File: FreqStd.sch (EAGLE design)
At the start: 33 parts, among them J1 ISP Connector, J2 BNC_RIGHT-ANGLE, SW1 PWR, U1 ATMEGA328, U2 MIC5205, U3 SN74LV164APW

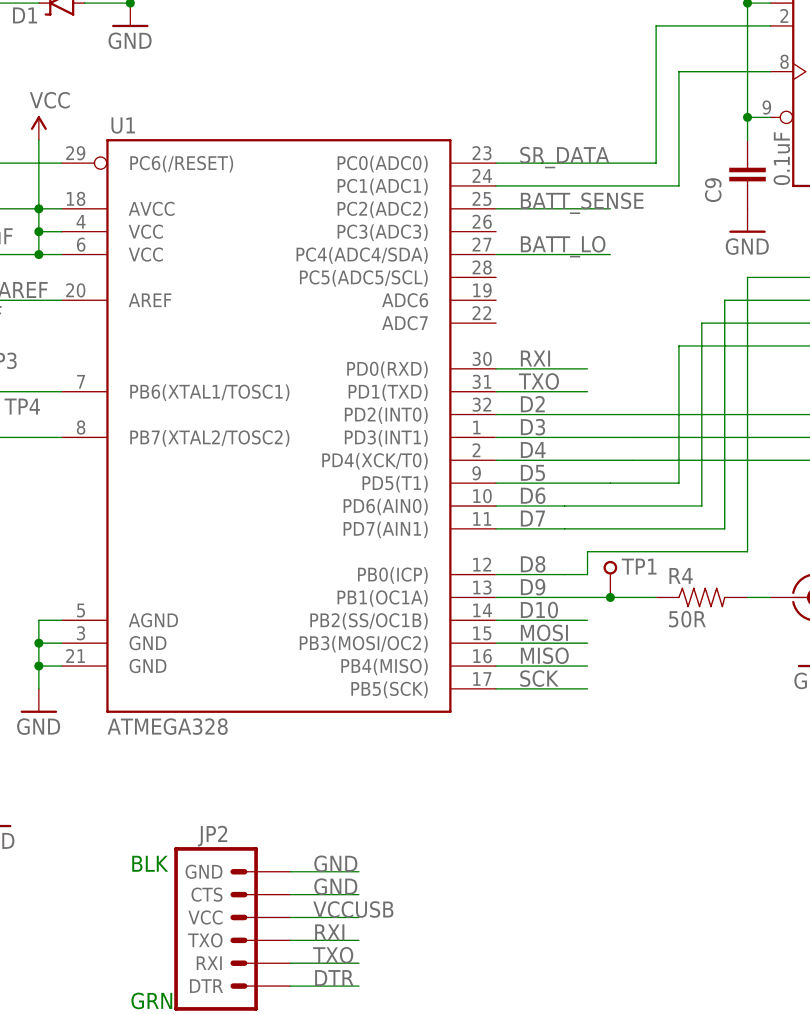
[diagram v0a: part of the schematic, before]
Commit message: Rev A board as ordered
Minor changes for ordering.  Added OSHPark renderings.  Started writing
firmware and GitHub cover.
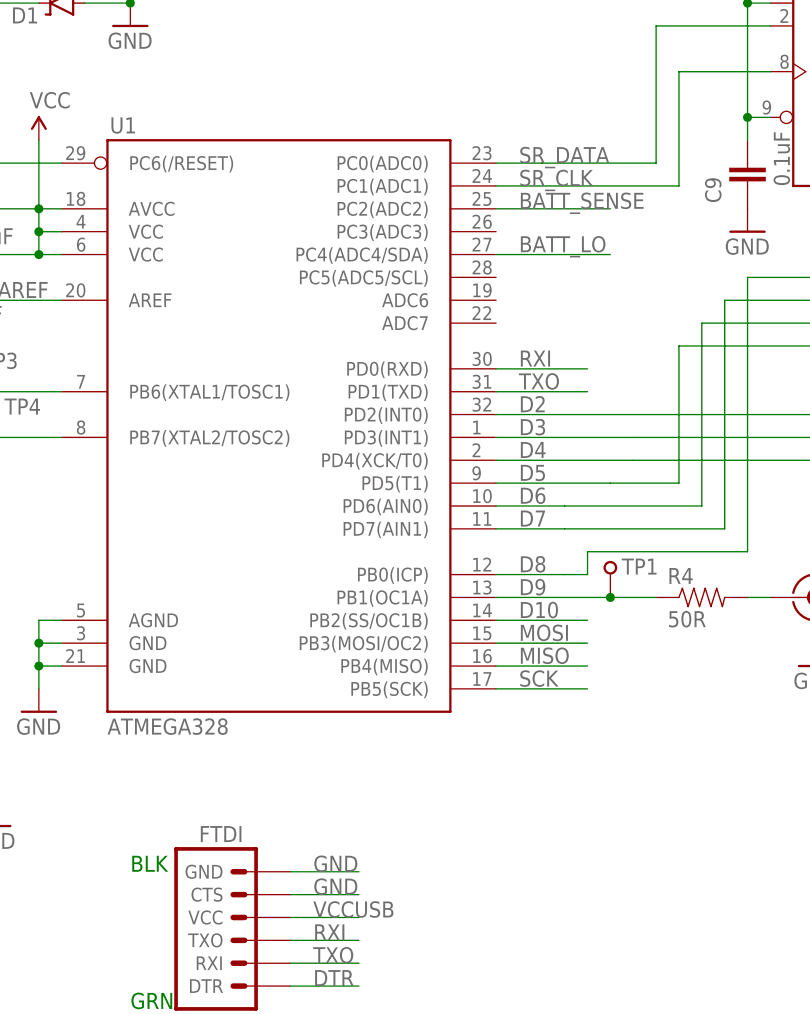
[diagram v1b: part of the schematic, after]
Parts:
- FRAME1: DATECODE 27AUG2015 -> 02SEP2015
- renumbered JP2 to FTDI
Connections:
- net N$7 renamed SR_CLK
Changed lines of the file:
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@@
 <?xml version="1.0" encoding="utf-8"?>
 <!DOCTYPE eagle SYSTEM "eagle.dtd">
-<eagle version="7.3.0">
+<eagle version="7.4.0">
 <drawing>
 <settings>
@@
 <part name="SUPPLY4" library="SparkFun-Aesthetics" deviceset="VCC" device="" value="VCC"/>
 <part name="GND4" library="SparkFun" deviceset="GND" device=""/>
-<part name="JP2" library="SparkFun" deviceset="ARDUINO_SERIAL_PROGRAM" device="PTH" value="FTDI Basic"/>
+<part name="FTDI" library="SparkFun" deviceset="ARDUINO_SERIAL_PROGRAM" device="PTH" value="FTDI Basic"/>
 <part name="J1" library="SparkFun-Connectors" deviceset="AVR_SPI_PRG_6" device="PTH" value="ISP Connector"/>
 <part name="SUPPLY3" library="SparkFun-Aesthetics" deviceset="VCC" device="" value="VCC"/>
@@
 <attribute name="CNAME" value="Frequency Standard"/>
 <attribute name="CREVISION" value="Rev A"/>
-<attribute name="DATECODE" value="27AUG2015"/>
+<attribute name="DATECODE" value="02SEP2015"/>
 <attribute name="DESIGNER" value="C.Schnarel"/>
 </part>
@@
 <instance part="SUPPLY4" gate="G$1" x="63.5" y="116.84"/>
 <instance part="GND4" gate="1" x="63.5" y="53.34"/>
-<instance part="JP2" gate="G$1" x="86.36" y="27.94"/>
+<instance part="FTDI" gate="G$1" x="86.36" y="27.94"/>
 <instance part="J1" gate="G$1" x="40.64" y="50.8"/>
 <instance part="SUPPLY3" gate="G$1" x="53.34" y="55.88"/>
@@
 <wire x1="91.44" y1="33.02" x2="99.06" y2="33.02" width="0.1524" layer="91"/>
 <label x="93.98" y="33.02" size="1.778" layer="95"/>
-<pinref part="JP2" gate="G$1" pin="CTS"/>
+<pinref part="FTDI" gate="G$1" pin="CTS"/>
 </segment>
 <segment>
 <wire x1="91.44" y1="35.56" x2="99.06" y2="35.56" width="0.1524" layer="91"/>
 <label x="93.98" y="35.56" size="1.778" layer="95"/>
-<pinref part="JP2" gate="G$1" pin="GND"/>
+<pinref part="FTDI" gate="G$1" pin="GND"/>
 </segment>
 <segment>
@@
 <wire x1="91.44" y1="25.4" x2="99.06" y2="25.4" width="0.1524" layer="91"/>
 <label x="93.98" y="25.4" size="1.778" layer="95"/>
-<pinref part="JP2" gate="G$1" pin="RXI"/>
+<pinref part="FTDI" gate="G$1" pin="RXI"/>
 </segment>
 </net>
@@
 <wire x1="91.44" y1="22.86" x2="99.06" y2="22.86" width="0.1524" layer="91"/>
 <label x="93.98" y="22.86" size="1.778" layer="95"/>
-<pinref part="JP2" gate="G$1" pin="DTR"/>
+<pinref part="FTDI" gate="G$1" pin="DTR"/>
 </segment>
 <segment>
@@
 <wire x1="91.44" y1="27.94" x2="99.06" y2="27.94" width="0.1524" layer="91"/>
 <label x="93.98" y="27.94" size="1.778" layer="95"/>
-<pinref part="JP2" gate="G$1" pin="TXO"/>
+<pinref part="FTDI" gate="G$1" pin="TXO"/>
 </segment>
 <segment>
@@
 </segment>
 <segment>
-<pinref part="JP2" gate="G$1" pin="VCC"/>
+<pinref part="FTDI" gate="G$1" pin="VCC"/>
 <wire x1="91.44" y1="30.48" x2="99.06" y2="30.48" width="0.1524" layer="91"/>
 <label x="93.98" y="30.48" size="1.778" layer="95"/>
@@
 </segment>
 </net>
-<net name="N$7" class="0">
+<net name="SR_CLK" class="0">
 <segment>
 <pinref part="U3" gate="G$1" pin="CLK"/>
@@
 <pinref part="U1" gate="G$1" pin="PC1(ADC1)"/>
 <wire x1="134.62" y1="111.76" x2="114.3" y2="111.76" width="0.2032" layer="91"/>
-</segment>
-</net>
+<label x="116.84" y="111.76" size="1.778" layer="95"/>
+</segment>
+</net>
